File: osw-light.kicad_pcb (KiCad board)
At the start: 4 copper layers, 36.1 x 36.1 mm, 55 parts, among them J1 Conn_01x02, Q1 2N7002, SW1 SW_Push, SW2 SW_Push, SW4 SW_Push, SW5 SW_Push, U1 DS3231MZ, U10 XC6209, U11 MCP73831T-2ACI_OT, U13 XC6209, U2 BMA400, U4 GC9A01_IPS_display, U5 USB-OTG, U6 CH340E, U7 ttgo-32-micro, U9 TPS2115A

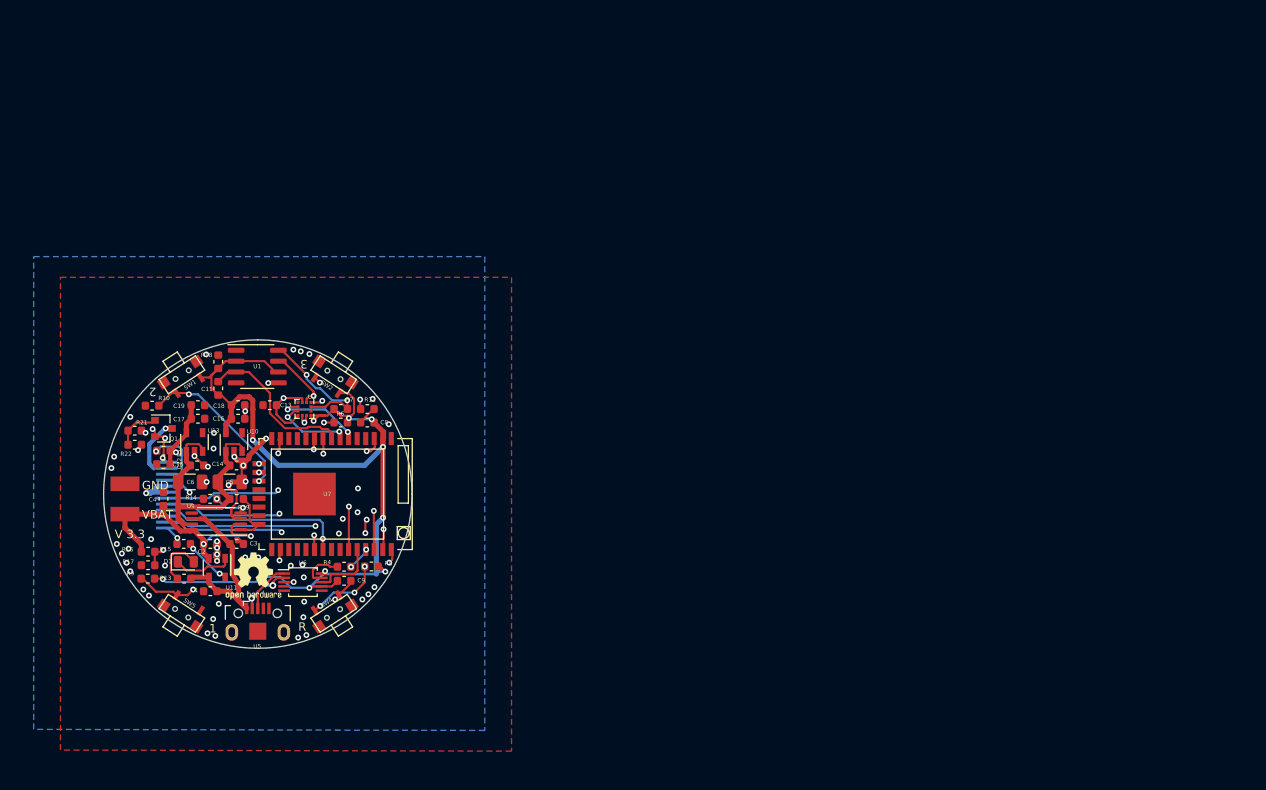
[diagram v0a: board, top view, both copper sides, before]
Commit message: Updated CAD and rough PCB in KiCAD
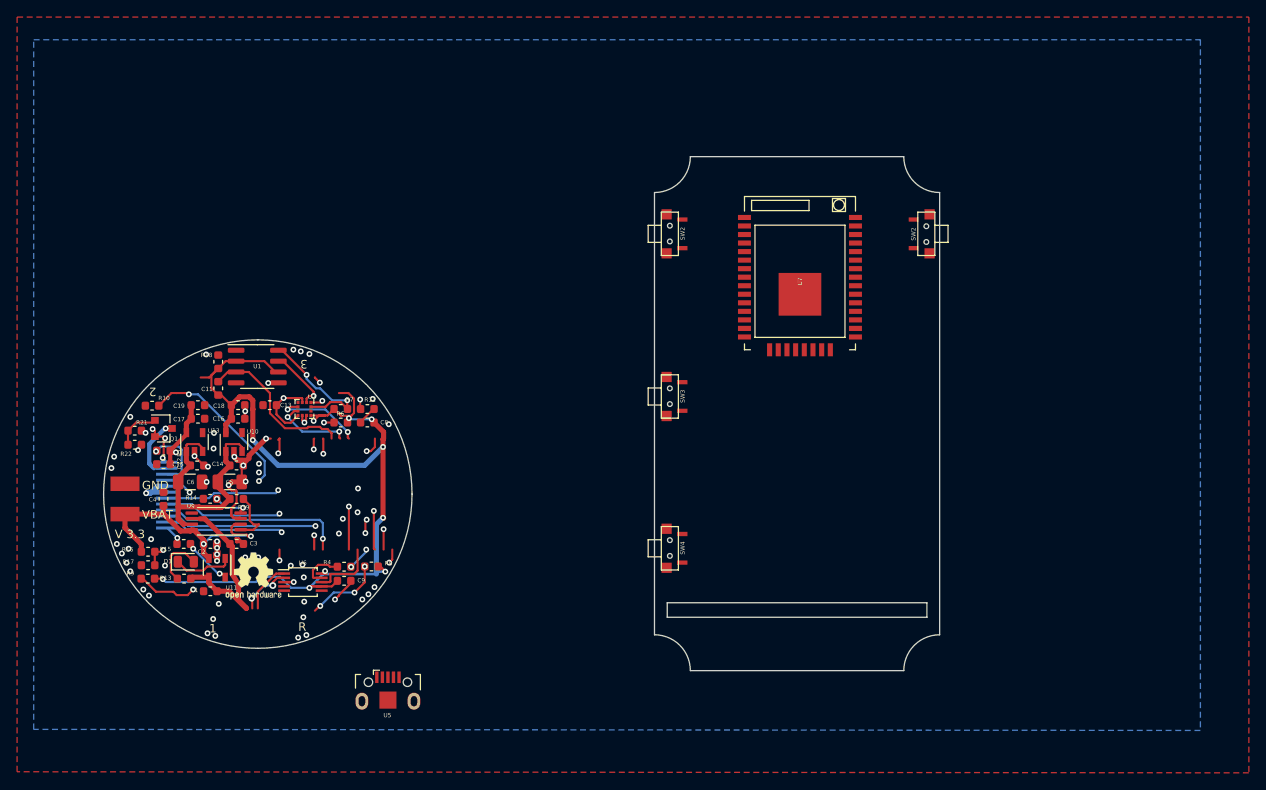
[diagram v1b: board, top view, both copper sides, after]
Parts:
- removed SW1, SW5: SW_Push, open-Smartwatch:button_side_smd
- removed the SW2 at (85.1, 87.6)
- added SW2: SW_Push, open-Smartwatch:button_side_smd, F.Cu at (154.5, 71.1)
- added SW2: SW_Push, open-Smartwatch:button_side_smd, F.Cu at (124.5, 71.1)
- added SW3: SW_Push, open-Smartwatch:button_side_smd, F.Cu at (124.5, 90.2)
- moved U7 60.5 mm to (139.7, 76.2), turned to 0 degrees
- moved SW4 40.1 mm to (124.5, 108.0), turned to 180 degrees
- moved U5 17.2 mm to (91.4, 125.7)
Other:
- board size 36.1 x 36.1 mm -> 97.9 x 60.2 mm

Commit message: Autosave
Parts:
- U4: moved to F.Cu
- moved U5 59.3 mm to (143.3, 97.0)
- moved U4 37.5 mm to (102.7, 100.1)
- moved REF** 33.1 mm to (108.2, 117.6)
- moved U9 13.2 mm to (76.2, 117.1)
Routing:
- net GND: track 64.5 -> 107.0 mm, vias 65 -> 67
- net /TFT_RST: track 29.6 -> 0.11 mm, vias 2 -> 1
- net /MOSI: track 28.4 -> 0.00 mm, vias 2 -> 0
- net /SCK: track 22.0 -> 0.00 mm, vias 1 -> 0
- net /3V3_2: track 17.5 -> 37.3 mm, vias 2 -> 4
- net /TFT_CS: track 20.6 -> 29.6 mm
- net /TFT_DC: track 19.8 -> 28.4 mm

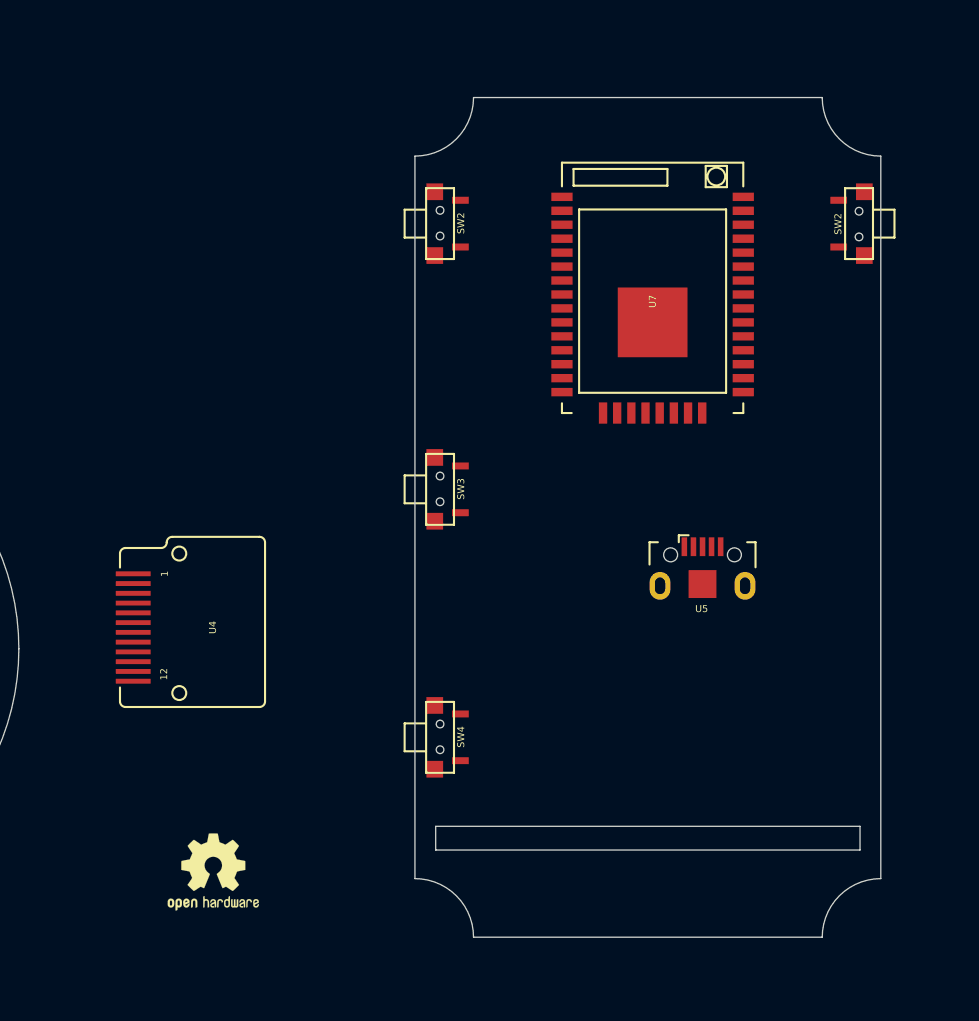
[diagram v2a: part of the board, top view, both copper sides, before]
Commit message: Updated PCB and removed unneeded models.
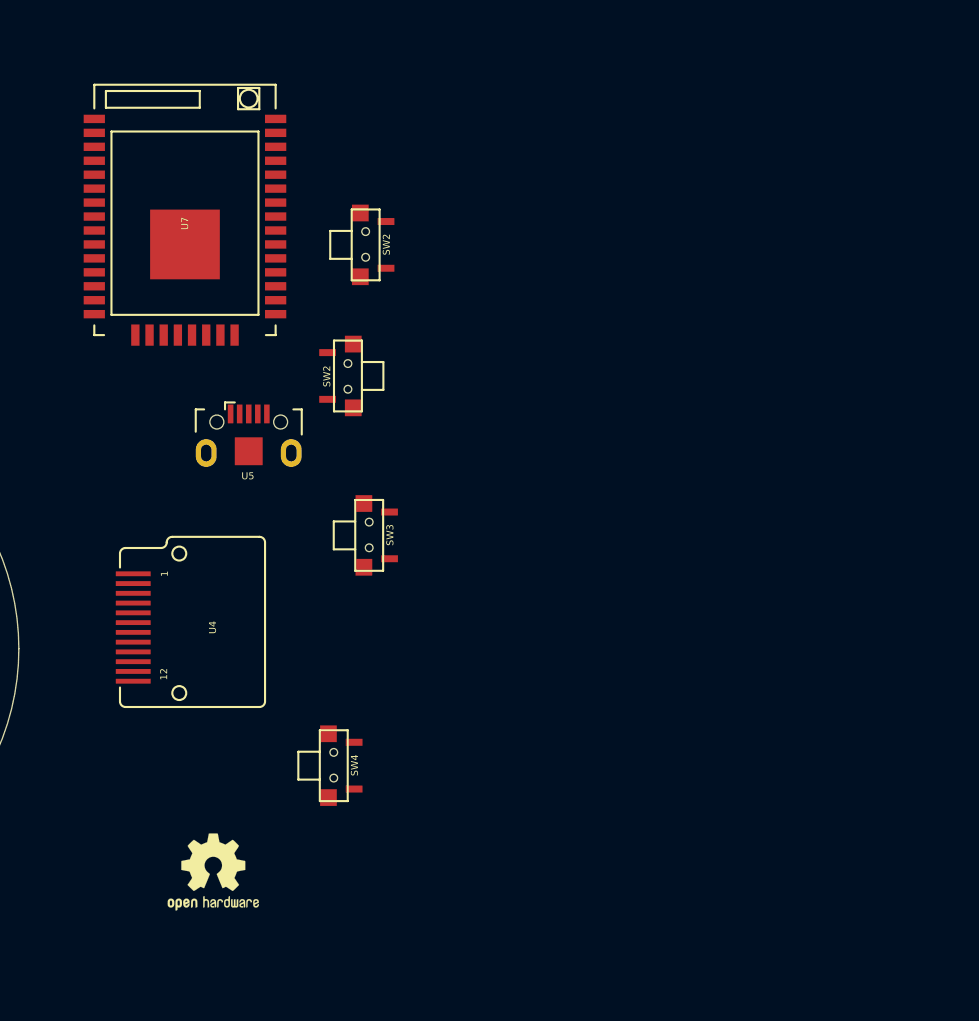
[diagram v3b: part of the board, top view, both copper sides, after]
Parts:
- moved SW2 38.2 mm to (117.9, 82.0)
- moved U7 34.0 mm to (106.2, 70.6)
- moved U5 33.9 mm to (110.7, 87.4)
- moved SW4 7.89 mm to (116.8, 110.0)
- moved SW3 6.06 mm to (119.4, 93.5)
- moved SW2 5.55 mm to (119.1, 72.6)
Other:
- board size 97.9 x 60.2 mm -> 36.1 x 36.1 mm
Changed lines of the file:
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@@
   (net 60 "Net-(U7-Pad12)")
   (footprint "open-Smartwatch:button_side_smd" (layer "F.Cu")
-    (at 124.46 107.95 180)
+    (at 116.84 109.982 180)
     (attr through_hole)
     (fp_text reference "SW4" (at -1.500326 0.025116 90) (layer "F.SilkS")
@@
   )
   (footprint "open-Smartwatch:USBmicro-B" (layer "F.Cu")
-    (at 143.2776 96.9615)
+    (at 110.744 87.4395)
     (solder_mask_margin 0.05)
     (attr through_hole)
@@
   )
   (footprint "open-Smartwatch:ttgo-32-micro" (layer "F.Cu")
-    (at 139.7 76.2)
+    (at 106.172 70.612)
     (attr through_hole)
     (fp_text reference "U7" (at 0 0.5 90) (layer "F.SilkS")
@@
   )
   (footprint "open-Smartwatch:button_side_smd" (layer "F.Cu")
-    (at 124.46 90.17 180)
+    (at 119.38 93.472 180)
     (attr through_hole)
     (fp_text reference "SW3" (at -1.500326 0.025116 90) (layer "F.SilkS")
@@
       (effects (font (size 0.5 0.5) (thickness 0.1)))
     )
-    (fp_line (start 1 2.54) (end 1 -2.54) (layer "F.SilkS") (width 0.15))
-    (fp_line (start 1 -1) (end 2.54 -1) (layer "F.SilkS") (width 0.15))
-    (fp_line (start 1 -2.54) (end -1 -2.54) (layer "F.SilkS") (width 0.15))
     (fp_line (start -1 2.54) (end 1 2.54) (layer "F.SilkS") (width 0.15))
+    (fp_line (start 1 -1) (end 2.54 -1) (layer "F.SilkS") (width 0.15))
+    (fp_line (start 1 2.54) (end 1 -2.54) (layer "F.SilkS") (width 0.15))
     (fp_line (start 2.54 1) (end 1 1) (layer "F.SilkS") (width 0.15))
-    (fp_line (start -1 -2.54) (end -1 2.54) (layer "F.SilkS") (width 0.15))
+    (fp_line (start 1 -2.54) (end -1 -2.54) (layer "F.SilkS") (width 0.15))
     (fp_line (start 2.54 -1) (end 2.54 1) (layer "F.SilkS") (width 0.15))
-    (pad "" np_thru_hole circle locked (at 0 0.9525 270) (size 0.55 0.55) (drill 0.55) (layers *.Mask "F.Cu" "In1.Cu" "In2.Cu" "B.Cu"))
+    (fp_line (start -1 -2.54) (end -1 2.54) (layer "F.SilkS") (width 0.15))
     (pad "" np_thru_hole circle locked (at 0 -0.889 180) (size 0.55 0.55) (drill 0.55) (layers *.Mask "F.Cu" "In1.Cu" "In2.Cu" "B.Cu"))
     (pad "" smd rect locked (at 0.381 2.286 180) (size 1.2 1.2) (layers "F.Cu" "F.Paste" "F.Mask"))
+    (pad "" np_thru_hole circle locked (at 0 0.9525 270) (size 0.55 0.55) (drill 0.55) (layers *.Mask "F.Cu" "In1.Cu" "In2.Cu" "B.Cu"))
     (pad "" smd rect locked (at 0.381 -2.286 180) (size 1.2 1.2) (layers "F.Cu" "F.Paste" "F.Mask"))
     (pad "1" smd rect locked (at -1.4605 -1.675 180) (size 1.2 0.5) (layers "F.Cu" "F.Paste" "F.Mask"))
@@
   )
   (footprint "open-Smartwatch:button_side_smd" (layer "F.Cu")
-    (at 154.5 71.12)
+    (at 117.856 82.042)
     (attr through_hole)
     (fp_text reference "SW2" (at -1.500326 0.025116 90) (layer "F.SilkS")
@@
       (effects (font (size 0.5 0.5) (thickness 0.1)))
     )
-    (fp_line (start 1 2.54) (end 1 -2.54) (layer "F.SilkS") (width 0.15))
-    (fp_line (start 1 -1) (end 2.54 -1) (layer "F.SilkS") (width 0.15))
+    (fp_line (start -1 -2.54) (end -1 2.54) (layer "F.SilkS") (width 0.15))
+    (fp_line (start 2.54 1) (end 1 1) (layer "F.SilkS") (width 0.15))
     (fp_line (start 1 -2.54) (end -1 -2.54) (layer "F.SilkS") (width 0.15))
     (fp_line (start -1 2.54) (end 1 2.54) (layer "F.SilkS") (width 0.15))
-    (fp_line (start 2.54 1) (end 1 1) (layer "F.SilkS") (width 0.15))
-    (fp_line (start -1 -2.54) (end -1 2.54) (layer "F.SilkS") (width 0.15))
+    (fp_line (start 1 -1) (end 2.54 -1) (layer "F.SilkS") (width 0.15))
+    (fp_line (start 1 2.54) (end 1 -2.54) (layer "F.SilkS") (width 0.15))
     (fp_line (start 2.54 -1) (end 2.54 1) (layer "F.SilkS") (width 0.15))
-    (pad "" np_thru_hole circle locked (at 0 0.9525 90) (size 0.55 0.55) (drill 0.55) (layers *.Mask "F.Cu" "In1.Cu" "In2.Cu" "B.Cu"))
+    (pad "" smd rect locked (at 0.381 -2.286) (size 1.2 1.2) (layers "F.Cu" "F.Paste" "F.Mask"))
     (pad "" np_thru_hole circle locked (at 0 -0.889) (size 0.55 0.55) (drill 0.55) (layers *.Mask "F.Cu" "In1.Cu" "In2.Cu" "B.Cu"))
     (pad "" smd rect locked (at 0.381 2.286) (size 1.2 1.2) (layers "F.Cu" "F.Paste" "F.Mask"))
-    (pad "" smd rect locked (at 0.381 -2.286) (size 1.2 1.2) (layers "F.Cu" "F.Paste" "F.Mask"))
+    (pad "" np_thru_hole circle locked (at 0 0.9525 90) (size 0.55 0.55) (drill 0.55) (layers *.Mask "F.Cu" "In1.Cu" "In2.Cu" "B.Cu"))
     (pad "1" smd rect locked (at -1.4605 -1.675) (size 1.2 0.5) (layers "F.Cu" "F.Paste" "F.Mask"))
     (pad "2" smd rect locked (at -1.4605 1.675) (size 1.2 0.5) (layers "F.Cu" "F.Paste" "F.Mask"))
   )
   (footprint "open-Smartwatch:button_side_smd" (layer "F.Cu")
-    (at 124.46 71.12 180)
+    (at 119.126 72.644 180)
     (attr through_hole)
     (fp_text reference "SW2" (at -1.500326 0.025116 90) (layer "F.SilkS")
@@
       (effects (font (size 0.5 0.5) (thickness 0.1)))
     )
-    (fp_line (start 1 2.54) (end 1 -2.54) (layer "F.SilkS") (width 0.15))
-    (fp_line (start 1 -1) (end 2.54 -1) (layer "F.SilkS") (width 0.15))
     (fp_line (start 1 -2.54) (end -1 -2.54) (layer "F.SilkS") (width 0.15))
-    (fp_line (start -1 2.54) (end 1 2.54) (layer "F.SilkS") (width 0.15))
     (fp_line (start 2.54 1) (end 1 1) (layer "F.SilkS") (width 0.15))
-    (fp_line (start -1 -2.54) (end -1 2.54) (layer "F.SilkS") (width 0.15))
     (fp_line (start 2.54 -1) (end 2.54 1) (layer "F.SilkS") (width 0.15))
+    (fp_line (start -1 2.54) (end 1 2.54) (layer "F.SilkS") (width 0.15))
+    (fp_line (start 1 -1) (end 2.54 -1) (layer "F.SilkS") (width 0.15))
+    (fp_line (start -1 -2.54) (end -1 2.54) (layer "F.SilkS") (width 0.15))
+    (fp_line (start 1 2.54) (end 1 -2.54) (layer "F.SilkS") (width 0.15))
     (pad "" np_thru_hole circle locked (at 0 0.9525 270) (size 0.55 0.55) (drill 0.55) (layers *.Mask "F.Cu" "In1.Cu" "In2.Cu" "B.Cu"))
-    (pad "" np_thru_hole circle locked (at 0 -0.889 180) (size 0.55 0.55) (drill 0.55) (layers *.Mask "F.Cu" "In1.Cu" "In2.Cu" "B.Cu"))
     (pad "" smd rect locked (at 0.381 2.286 180) (size 1.2 1.2) (layers "F.Cu" "F.Paste" "F.Mask"))
+    (pad "" np_thru_hole circle locked (at 0 -0.889 180) (size 0.55 0.55) (drill 0.55) (layers *.Mask "F.Cu" "In1.Cu" "In2.Cu" "B.Cu"))
     (pad "" smd rect locked (at 0.381 -2.286 180) (size 1.2 1.2) (layers "F.Cu" "F.Paste" "F.Mask"))
     (pad "1" smd rect locked (at -1.4605 -1.675 180) (size 1.2 0.5) (layers "F.Cu" "F.Paste" "F.Mask"))
@@
   (gr_line (start 76.2 76.2) (end 76.2 127) (layer "Dwgs.User") (width 0.05))
   (gr_line (start 56.007 101.6) (end 56.007 108.204) (layer "Dwgs.User") (width 0.12))
-  (gr_arc (start 156.06 66.28) (mid 153.090152 65.049848) (end 151.86 62.08) (layer "Edge.Cuts") (width 0.05))
-  (gr_arc (start 151.86 122.28) (mid 153.090152 119.310152) (end 156.06 118.08) (layer "Edge.Cuts") (width 0.05))
-  (gr_arc (start 126.86 62.08) (mid 125.629848 65.049848) (end 122.66 66.28) (layer "Edge.Cuts") (width 0.05))
-  (gr_rect (start 124.15 114.33) (end 154.57 116.03) (layer "Edge.Cuts") (width 0.05) (fill none))
   (gr_arc (start 76.2 83.537403) (mid 88.972185 88.827815) (end 94.262597 101.6) (layer "Edge.Cuts") (width 0.05))
   (gr_arc (start 76.2 119.662597) (mid 63.427815 114.372185) (end 58.137403 101.6) (layer "Edge.Cuts") (width 0.05))
-  (gr_line (start 156.06 66.28) (end 156.06 118.08) (layer "Edge.Cuts") (width 0.05))
-  (gr_line (start 122.66 66.28) (end 122.66 118.08) (layer "Edge.Cuts") (width 0.05))
   (gr_arc (start 94.262597 101.6) (mid 88.972185 114.372185) (end 76.2 119.662597) (layer "Edge.Cuts") (width 0.05))
-  (gr_line (start 151.86 122.28) (end 126.86 122.28) (layer "Edge.Cuts") (width 0.05))
-  (gr_arc (start 122.66 118.08) (mid 125.629848 119.310152) (end 126.86 122.28) (layer "Edge.Cuts") (width 0.05))
   (gr_arc (start 58.137403 101.6) (mid 63.427815 88.827815) (end 76.2 83.537403) (layer "Edge.Cuts") (width 0.05))
-  (gr_line (start 126.86 62.08) (end 151.86 62.08) (layer "Edge.Cuts") (width 0.05))
   (gr_text "1" (at 67.056 115.7605 -33) (layer "B.SilkS")
     (effects (font (size 1 1) (thickness 0.2)) (justify mirror))
@@
     )
   )
-  (group "" (id b528d586-96d5-447f-8be4-09de71021e5e)
-    (members
-      028c6ceb-bae6-4a26-ba66-57ec77ec021a
-      1831153e-da27-4513-9ea4-bd6aec82148a
-      1af65e33-a64f-423d-b3df-b63fe3de0bf0
-      1db25eb4-805a-4bd2-8268-61bee83a7d3f
-      81419874-c5da-47de-8f94-360bffbdf078
-      8a5f5652-9146-4b50-8fb8-430ecaeaebe8
-      af29991f-8582-4bb5-9ea3-196e21438550
-      b8ef0302-2436-4dd3-9da0-57b8f75d6222
-      f76946ea-32ff-43a6-a450-c7bda513b9d8
-    )
-  )
